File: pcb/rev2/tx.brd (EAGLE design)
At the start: 28 x 36.5 mm, 54 parts, among them U3 MCP73831T-2ACI/OT, Y1 CRYSTAL-26MHZSMD-3.2X2.5

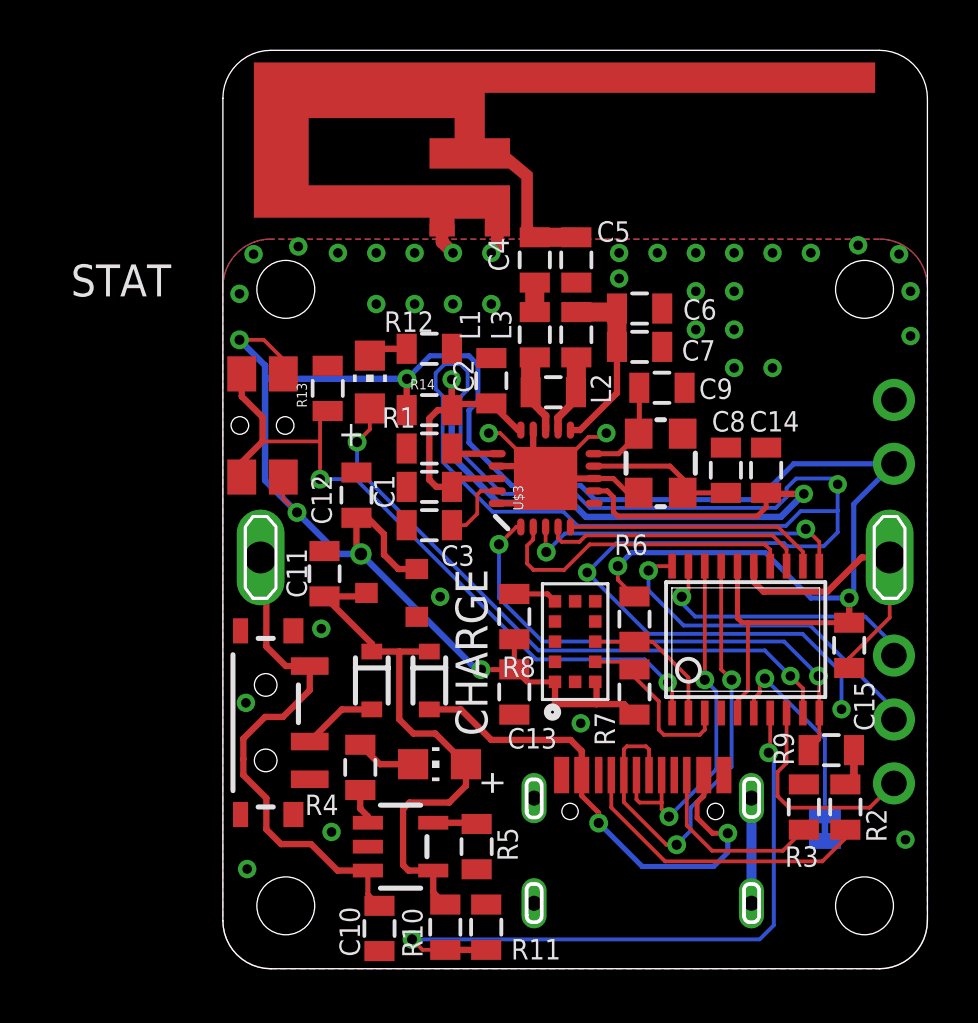
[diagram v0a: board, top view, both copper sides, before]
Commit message: added more power filtering, added RX interrupt
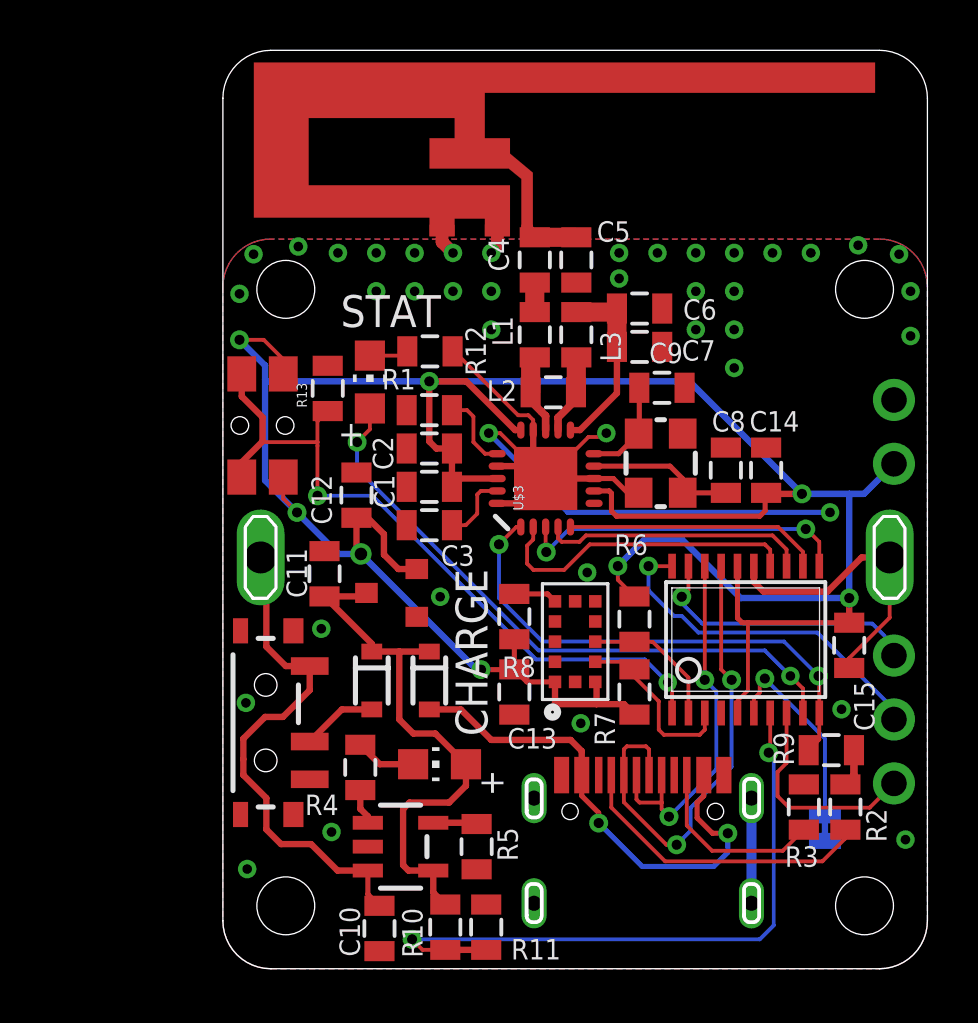
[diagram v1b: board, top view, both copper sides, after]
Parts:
- removed R14: 1 Ohm, joyAnalog:0805
- moved C2 3.65 mm to (8.20, 20.7), turned to 180 degrees
- moved R1 1.52 mm to (8.20, 22.2)
- moved R12 0.10 mm to (8.23, 24.5)
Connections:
- removed net N$37: C1.1, C14.1, C2.1, R14.2, U$3.15, U$3.18, U$3.7
- net +3V3: now also C1.1, C14.1, C2.1, U$3.15, U$3.18, U$3.7; no longer R14.1
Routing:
- net GND: track 102.7 -> 54.3 mm
- net N$37: track 39.2 -> 0.00 mm, vias 2 -> 0
- net +3V3: track 97.6 -> 112.8 mm, vias 7 -> 8
- net N$2: track 1.88 -> 3.11 mm
